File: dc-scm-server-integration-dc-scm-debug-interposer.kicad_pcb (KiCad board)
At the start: 6 copper layers, 90 x 62.3 mm, 164 parts, among them J1 Socket_DC-SCM-2.1_2x84_Rev-1-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, J10 PinHeader_2x5_P2.54mm_SMD, J11 PinHeader_2x5_P2.54mm_SMD, J12 PinHeader_2x5_P2.54mm_SMD, J13 PinHeader_2x5_P2.54mm_SMD, J15 Socket_SOP2-16_ACA-SPI-006-K0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, J16 Socket_SOP2-16_ACA-SPI-006-K0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, J17 PinHeader_2x5_P2.54mm_SMD, J2 PCB-Edge_DC-SCM-2.1_2x84_Rev-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, J3 PinHeader_2x5_P2.54mm_SMD, J4 PinHeader_2x5_P2.54mm_SMD, J5 PinHeader_2x5_P2.54mm_SMD, J6 PinHeader_2x5_P2.54mm_SMD, J7 PinHeader_2x5_P2.54mm_SMD, J9 PinHeader_2x5_P2.54mm_SMD, Q3 DMG1012T-7, U1 TLV76701_WSON

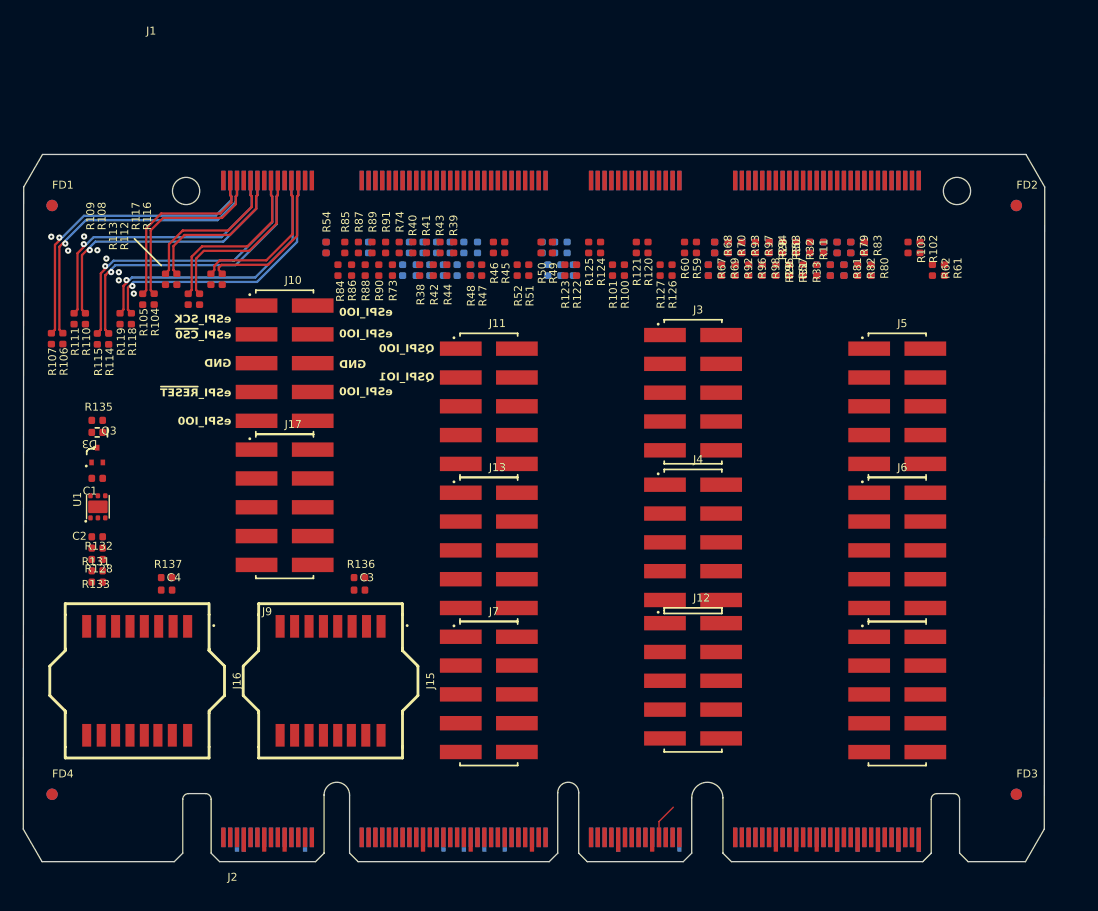
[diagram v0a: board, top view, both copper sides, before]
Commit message: [#100720] Start placing silkscreen labels
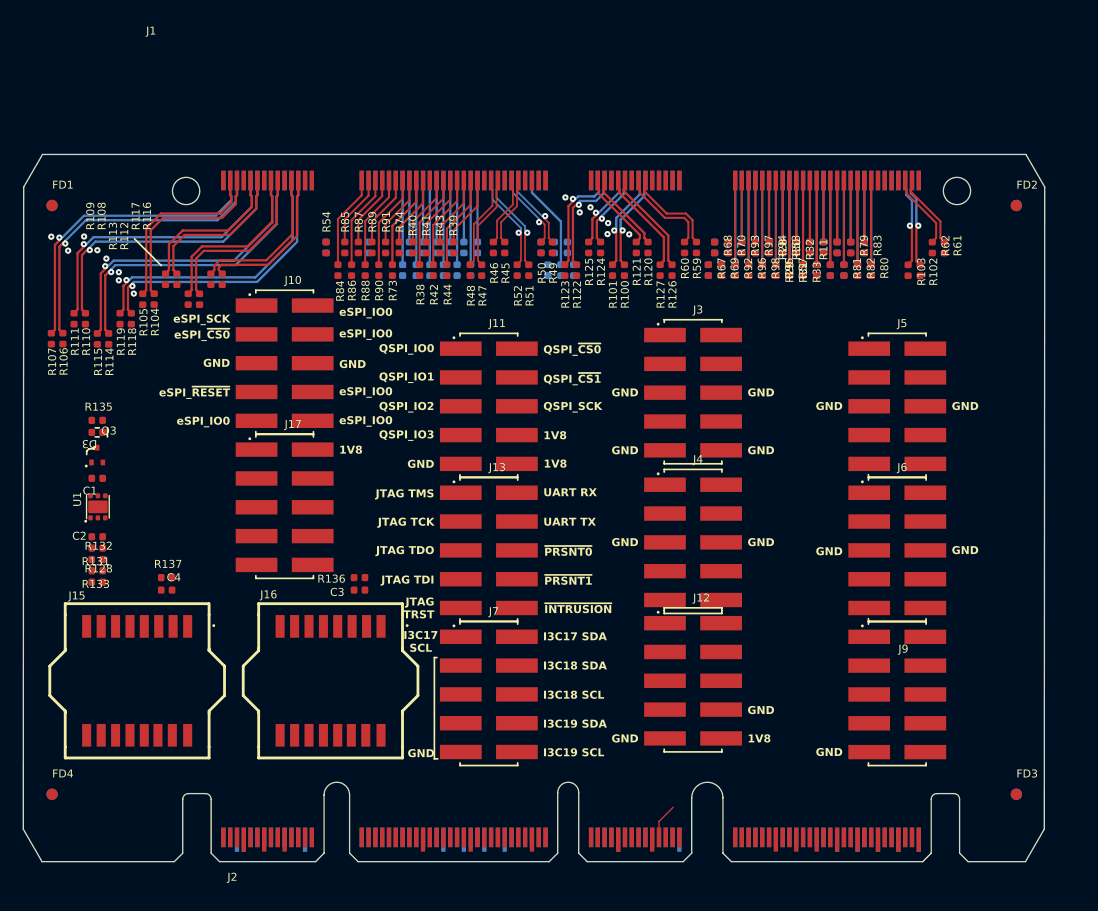
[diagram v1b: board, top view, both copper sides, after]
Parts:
- moved R102 2.01 mm to (179.0, 80.2)
- moved R103 2.01 mm to (178.0, 80.2)
- moved R61 1.99 mm to (181.1, 78.2)
- moved R62 1.99 mm to (180.1, 78.2)
- moved R3 0.10 mm to (145.6, 78.2)
- turned R99 to 90 degrees
- turned R14 to 90 degrees
- turned R15 to 90 degrees
- turned R16 to 90 degrees
- turned R18 to 90 degrees
- turned R20 to 90 degrees
- turned R21 to 90 degrees
- turned R22 to 90 degrees
- turned R23 to 90 degrees
- turned R24 to 90 degrees
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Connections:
- net Net-(J1A-USB2_SCMHOST1_DN) renamed /DC-SCI gold fingers connector/USB1_D-
- net Net-(J1A-USB2_SCMHOST1_DP) renamed /DC-SCI gold fingers connector/USB1_D+
- net Net-(J1A-USB2_SCMHOST2_DN) renamed /DC-SCI gold fingers connector/USB2_D-
- net Net-(J1A-USB2_SCMHOST2_DP) renamed /DC-SCI gold fingers connector/USB2_D+
- net Net-(J1C-LTPI_HPM_SCM_CLK_DN) renamed /DC-SCI gold fingers connector/LTPI_RXCK-
- net Net-(J1C-LTPI_HPM_SCM_CLK_DP) renamed /DC-SCI gold fingers connector/LTPI_RXCK+
- net Net-(J1C-LTPI_HPM_SCM_DATA_DN) renamed /DC-SCI gold fingers connector/LTPI_RXD-
- net Net-(J1C-LTPI_HPM_SCM_DATA_DP) renamed /DC-SCI gold fingers connector/LTPI_RXD+
- net Net-(J1C-LTPI_SCM_HPM_CLK_DN) renamed /DC-SCI gold fingers connector/LTPI_TXCK-
- net Net-(J1C-LTPI_SCM_HPM_CLK_DP) renamed /DC-SCI gold fingers connector/LTPI_TXCK+
- net Net-(J1C-LTPI_SCM_HPM_DATA_DN) renamed /DC-SCI gold fingers connector/LTPI_TXD-
- net Net-(J1C-LTPI_SCM_HPM_DATA_DP) renamed /DC-SCI gold fingers connector/LTPI_TXD+
- J1 pad A68: /DC-SCI gold fingers connector/CLK_100M_1_CLK+ -> /DC-SCI gold fingers connector/CLK_100M_1_CLK-
- R103 pad 1: /DC-SCI gold fingers connector/CLK_100M_1_CLK+ -> /DC-SCI gold fingers connector/CLK_100M_1_CLK-
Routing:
- net /DC-SCI gold fingers connector/PCIE1_RX0-: track 0.00 -> 9.69 mm, vias 0 -> 1
- net /DC-SCI gold fingers connector/PCIE1_RX0+: track 0.00 -> 9.69 mm, vias 0 -> 1
- net /DC-SCI gold fingers connector/PCIE_USB_SCMROOT_TX0+: track 0.00 -> 9.23 mm
- net /DC-SCI gold fingers connector/PCIE_USB_SCMROOT_TX0-: track 0.00 -> 9.23 mm
- net /DC-SCI gold fingers connector/LTPI_TXD-: track 0.00 -> 8.81 mm, vias 0 -> 1
- net /DC-SCI gold fingers connector/LTPI_TXD+: track 0.00 -> 8.81 mm, vias 0 -> 1
- net /DC-SCI gold fingers connector/CLK_100M_0_CLK-: track 0.00 -> 8.60 mm, vias 0 -> 1
- net /DC-SCI gold fingers connector/CLK_100M_0_CLK+: track 0.00 -> 8.60 mm, vias 0 -> 1
- net Net-(J1B-I2C_3V3_2_SCL): track 0.00 -> 8.48 mm
- net /DC-SCI gold fingers connector/USB1_D-: track 0.00 -> 8.37 mm
- net /DC-SCI gold fingers connector/USB1_D+: track 0.00 -> 8.37 mm
- net Net-(J1C-QSPI_HPMCNTRL_IO_1): track 0.00 -> 8.29 mm
- net Net-(J1C-QSPI_HPMCNTRL_CS0_N): track 0.00 -> 8.29 mm
- net Net-(J1C-ESPI_HPMCNTRL_RESET_N): track 0.00 -> 8.29 mm
- net Net-(J1C-ESPI_HPMCNTRL_IO_3): track 0.00 -> 8.29 mm
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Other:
- board text added: "1V8"
- board text added: "I3C17 SCL"
- board text added: "I3C17 SDA"
- board text added: "I3C18 SCL"
- board text added: "I3C18 SDA"
- board text added: "I3C19 SCL"
- board text added: "I3C19 SDA"
- board text added: "JTAG TCK"
- board text added: "JTAG TDI"
- board text added: "JTAG TDO"
- board text added: "JTAG TMS"
- board text added: "JTAG TRST"
- board text added: "QSPI_IO2"
- board text added: "QSPI_IO3"
- board text added: "QSPI_SCK"
- board text added: "QSPI_~{CS0}"
- board text added: "QSPI_~{CS1}"
- board text added: "UART RX"
- board text added: "UART TX"
- board text added: "~{INTRUSION}"
- board text added: "~{PRSNT0}"
- board text added: "~{PRSNT1}"

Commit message: [#100720] Finish silkscreen
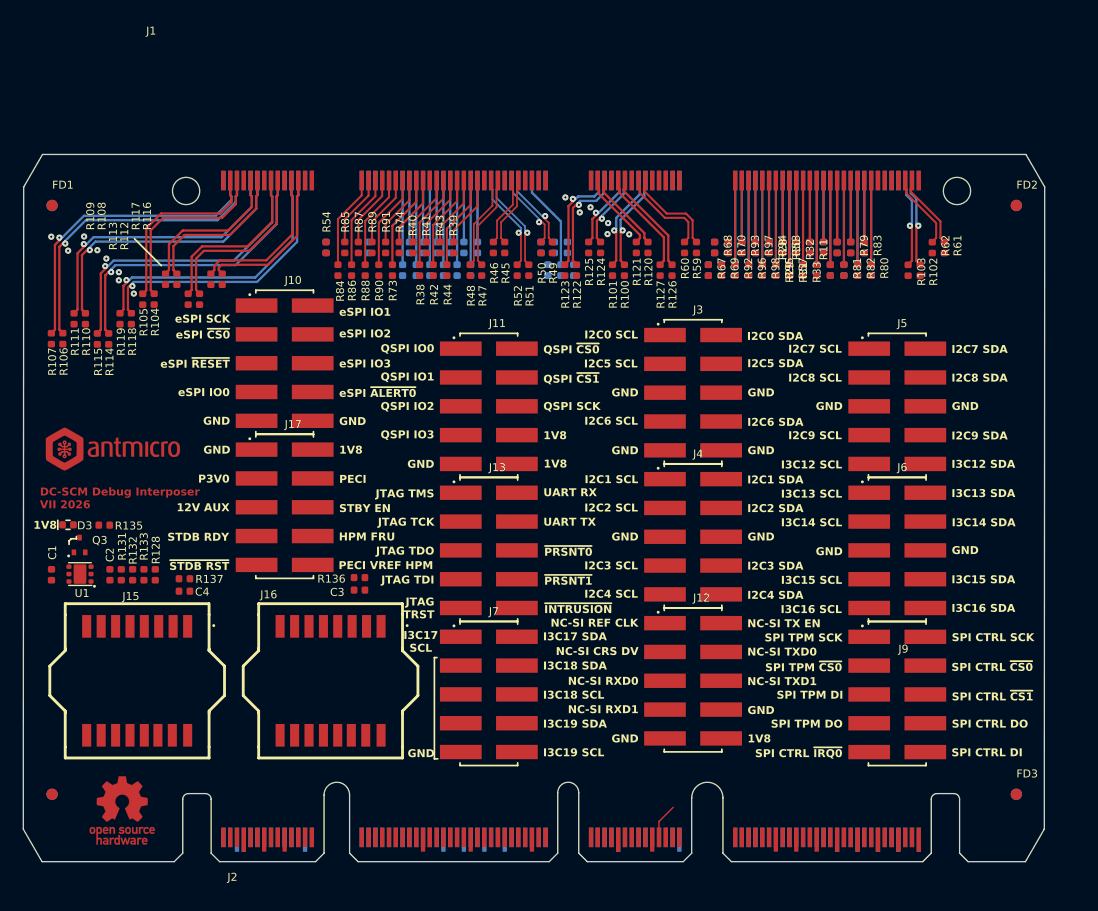
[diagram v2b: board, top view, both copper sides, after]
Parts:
- added REF**: OSHW-Logo_5.7x6mm_Copper, antmicro-footprints:OSHW-Logo_5.7x6mm_Copper, F.Cu at (108.7, 127.8)
- added REF**: LOGO, antmicro-footprints:antmicro-logo_scaled_12mm, F.Cu at (107.8, 96.0)
- added REF**: OSHW-Logo_5.7x6mm_Mask, antmicro-footprints:OSHW-Logo_5.7x6mm_Mask, F.Cu at (108.7, 127.8)
- moved C1 9.41 mm to (102.5, 107.0), turned to -90 degrees
- moved R135 9.26 mm to (107.1, 102.7)
- moved D3 8.55 mm to (103.9, 102.7), turned to 0 degrees
- moved Q3 8.08 mm to (104.9, 104.4)
- moved U1 6.14 mm to (105.0, 107.0), turned to 180 degrees
- moved R128 5.16 mm to (111.6, 107.0), turned to 90 degrees
- moved R133 4.13 mm to (110.6, 107.0), turned to -90 degrees
- moved C2 3.53 mm to (107.6, 107.0), turned to -90 degrees
- moved R132 3.40 mm to (109.6, 107.0), turned to 90 degrees
- moved R131 3.16 mm to (108.6, 107.0), turned to -90 degrees
- moved R137 1.57 mm to (114.2, 107.4)
- moved C4 1.57 mm to (114.2, 108.5)
- moved J4 0.49 mm to (159.0, 103.7)
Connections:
- J10 pad 10: /DC-SCI edge connector/DC_SCM_ESPI.~{ALERT0} -> GND
- J10 pad 5: GND -> /DC-SCI edge connector/DC_SCM_ESPI.~{RESET}
- J10 pad 6: GND -> /DC-SCI edge connector/DC_SCM_ESPI.IO3
- J10 pad 7: /DC-SCI edge connector/DC_SCM_ESPI.~{RESET} -> /DC-SCI edge connector/DC_SCM_ESPI.IO0
- J10 pad 8: /DC-SCI edge connector/DC_SCM_ESPI.IO3 -> /DC-SCI edge connector/DC_SCM_ESPI.~{ALERT0}
- J10 pad 9: /DC-SCI edge connector/DC_SCM_ESPI.IO0 -> GND
- J17 pad 1: /DC-SCI edge connector/DC_SCM_12V_AUX -> GND
- J17 pad 5: /DC-SCI edge connector/DC_SCM_STBY_RDY -> /DC-SCI edge connector/DC_SCM_12V_AUX
- J17 pad 7: /DC-SCI edge connector/~{DC_SCM_STBY_RST} -> /DC-SCI edge connector/DC_SCM_STBY_RDY
- J17 pad 9: /DC-SCI edge connector/~{DC_SCM_SPI_SCMCNTRL_IRQ0} -> /DC-SCI edge connector/~{DC_SCM_STBY_RST}
- J9 pad 9: GND -> /DC-SCI edge connector/~{DC_SCM_SPI_SCMCNTRL_IRQ0}
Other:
- board text added: "12V AUX"
- board text added: "DC-SCM Debug Interposer VII 2026"
- board text added: "HPM FRU"
- board text added: "I2C0 SCL"
- board text added: "I2C0 SDA"
- board text added: "I2C1 SCL"
- board text added: "I2C1 SDA"
- board text added: "I2C2 SCL"
- board text added: "I2C2 SDA"
- board text added: "I2C3 SCL"
- board text added: "I2C3 SDA"
- board text added: "I2C4 SCL"
- board text added: "I2C4 SDA"
- board text added: "I2C5 SCL"
- board text added: "I2C5 SDA"
- board text added: "I2C6 SCL"
- board text added: "I2C6 SDA"
- board text added: "I2C7 SCL"
- board text added: "I2C7 SDA"
- board text added: "I2C8 SCL"
- board text added: "I2C8 SDA"
- board text added: "I2C9 SCL"
- board text added: "I2C9 SDA"
- board text added: "I3C12 SCL"
- board text added: "I3C12 SDA"
- board text added: "I3C13 SCL"
- board text added: "I3C13 SDA"
- board text added: "I3C14 SCL"
- board text added: "I3C14 SDA"
- board text added: "I3C15 SCL"
- board text added: "I3C15 SDA"
- board text added: "I3C16 SCL"
- board text added: "I3C16 SDA"
- board text added: "NC-SI CRS DV"
- board text added: "NC-SI REF CLK"
- board text added: "NC-SI RXD0"
- board text added: "NC-SI RXD1"
- board text added: "NC-SI TX EN"
- board text added: "NC-SI TXD0"
- board text added: "NC-SI TXD1"
- board text added: "P3V0"
- board text added: "PECI"
- board text added: "PECI VREF HPM"
- board text added: "QSPI IO0"
- board text added: "QSPI IO1"
- board text added: "QSPI IO2"
- board text added: "QSPI IO3"
- board text added: "QSPI SCK"
- board text added: "QSPI ~{CS0}"
- board text added: "QSPI ~{CS1}"
- board text added: "SPI CTRL DI"
- board text added: "SPI CTRL DO"
- board text added: "SPI CTRL SCK"
- board text added: "SPI CTRL ~{CS0}"
- board text added: "SPI CTRL ~{CS1}"
- board text added: "SPI CTRL ~{IRQ0}"
- board text added: "SPI TPM DI"
- board text added: "SPI TPM DO"
- board text added: "SPI TPM SCK"
- board text added: "SPI TPM ~{CS0}"
- board text added: "STBY EN"
- board text added: "STDB RDY"
- board text added: "eSPI IO0"
- board text added: "eSPI IO1"
- board text added: "eSPI IO2"
- board text added: "eSPI IO3"
- board text added: "eSPI SCK"
- board text added: "eSPI ~{ALERT0}"
- board text added: "eSPI ~{CS0}"
- board text added: "eSPI ~{RESET}"
- board text added: "~{STDB RST}"
- board text removed: "QSPI_IO0"
- board text removed: "QSPI_IO1"
- board text removed: "QSPI_IO2"
- board text removed: "QSPI_IO3"
- board text removed: "QSPI_SCK"
- board text removed: "QSPI_~{CS0}"
- board text removed: "QSPI_~{CS1}"
- board text removed: "eSPI_IO0"
- board text removed: "eSPI_SCK"
- board text removed: "eSPI_~{CS0}"
- board text removed: "eSPI_~{RESET}"

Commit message: [#100720] Route high speeds
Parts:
- removed the REF** at (108.7, 127.8)
- J2: footprint antmicro-footprints:PCB-Edge_DC-SCM_2x84_Rev-1-0 -> antmicro-footprints:PCB-Edge_DC-SCM-2.1_2x84_Rev-1-1
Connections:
- J2 pad A51: /DC-SCI edge connector/DC_SCM_I2C_I3C16.SCL -> /DC-SCI edge connector/DC_SCM_I2C_I3C16.SDA
- J2 pad A52: /DC-SCI edge connector/DC_SCM_I2C_I3C16.SDA -> /DC-SCI edge connector/DC_SCM_I2C_I3C16.SCL
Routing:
- net /DC-SCI edge connector/DC_SCM_USB2.D-: track 0.00 -> 60.2 mm
- net /DC-SCI edge connector/DC_SCM_USB2.D+: track 0.00 -> 60.2 mm
- net /DC-SCI edge connector/DC_SCM_LTPI.RXCK+: track 0.00 -> 58.6 mm
- net /DC-SCI edge connector/DC_SCM_LTPI.RXCK-: track 0.00 -> 58.6 mm
- net /DC-SCI edge connector/DC_SCM_LTPI.RXD-: track 0.00 -> 57.1 mm
- net /DC-SCI edge connector/DC_SCM_LTPI.RXD+: track 0.00 -> 57.1 mm
- net /DC-SCI edge connector/DC-SCM_CLK_100M_1.CLK+: track 0.00 -> 56.8 mm, vias 0 -> 1
- net /DC-SCI edge connector/DC-SCM_CLK_100M_1.CLK-: track 0.00 -> 56.8 mm, vias 0 -> 1
- net /DC-SCI edge connector/DC-SCM_PCIE0_SGMII.RX1-: track 0.00 -> 56.5 mm, vias 0 -> 1
- net /DC-SCI edge connector/DC-SCM_PCIE0_SGMII.RX1+: track 0.00 -> 56.5 mm, vias 0 -> 1
- net /DC-SCI edge connector/DC-SCM_PCIE0_SGMII.RX3-: track 0.00 -> 55.9 mm, vias 0 -> 1
- net /DC-SCI edge connector/DC-SCM_PCIE0_SGMII.RX3+: track 0.00 -> 55.9 mm, vias 0 -> 1
- net /DC-SCI edge connector/DC_SCM_USB1.D-: track 0.00 -> 55.0 mm
- net /DC-SCI edge connector/DC_SCM_USB1.D+: track 0.00 -> 55.0 mm
- net /DC-SCI edge connector/DC-SCM_PCIE0_SGMII.RX0+: track 0.00 -> 54.9 mm, vias 0 -> 1
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
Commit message: [#100720] Start routing low speeds
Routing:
- net /DC-SCI edge connector/DC_SCM_HPM_FRU: track 0.00 -> 98.4 mm, vias 0 -> 2
- net /DC-SCI edge connector/DC_SCM_UART.TX: track 0.00 -> 82.8 mm, vias 0 -> 2
- net /DC-SCI edge connector/DC_SCM_UART.RX: track 0.00 -> 78.7 mm, vias 0 -> 2
- net /DC-SCI edge connector/DC_SCM_I2C_I3C18.SCL: track 0.00 -> 68.7 mm, vias 0 -> 2
- net /DC-SCI edge connector/DC_SCM_I2C_I3C19.SCL: track 0.00 -> 65.2 mm, vias 0 -> 2
- net /DC-SCI edge connector/DC_SCM_I2C_I3C18.SDA: track 0.00 -> 65.1 mm, vias 0 -> 2
- net /DC-SCI edge connector/DC_SCM_I2C_I3C19.SDA: track 0.00 -> 65.1 mm, vias 0 -> 2
- net /DC-SCI edge connector/DC_SCM_I2C7.SCL: track 0.00 -> 61.7 mm, vias 0 -> 2
- net /DC-SCI edge connector/DC_SCM_I2C7.SDA: track 0.00 -> 61.7 mm, vias 0 -> 2
- net /DC-SCI edge connector/DC_SCM_I2C_I3C16.SCL: track 0.00 -> 60.5 mm, vias 0 -> 2
- net /DC-SCI edge connector/DC_SCM_TPM_SPI.DI: track 0.00 -> 58.8 mm, vias 0 -> 2
- net /DC-SCI edge connector/DC_SCM_TPM_SPI.SCK: track 0.00 -> 58.6 mm, vias 0 -> 2
- net /DC-SCI edge connector/DC_SCM_I2C5.SCL: track 0.00 -> 58.4 mm, vias 0 -> 2
- net /DC-SCI edge connector/DC_SCM_I2C_I3C13.SDA: track 0.00 -> 58.0 mm, vias 0 -> 2
- net /DC-SCI edge connector/DC_SCM_I2C_I3C12.SDA: track 0.00 -> 57.6 mm, vias 0 -> 2
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
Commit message: [#100720] Continue routing low speeds
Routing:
- net GND: track 38.4 -> 138.9 mm, vias 42 -> 83
- net /DC-SCI edge connector/DC_SCM_STBY_EN: track 0.00 -> 78.9 mm, vias 0 -> 2
- net /DC-SCI edge connector/~{DC_SCM_STBY_RST}: track 0.00 -> 76.7 mm, vias 0 -> 2
- net /DC-SCI edge connector/DC_SCM_I2C_I3C14.SDA: track 0.00 -> 75.0 mm, vias 0 -> 4
- net /DC-SCI edge connector/DC_SCM_I2C0.SDA: track 0.00 -> 73.8 mm, vias 0 -> 2
- net /DC-SCI edge connector/DC_SCM_I2C_I3C15.SDA: track 0.00 -> 73.0 mm, vias 0 -> 4
- net /DC-SCI edge connector/DC_SCM_I2C0.SCL: track 0.00 -> 72.8 mm, vias 0 -> 2
- net /DC-SCI edge connector/DC_SCM_I2C1.SCL: track 0.00 -> 71.7 mm, vias 0 -> 2
- net /DC-SCI edge connector/DC_SCM_I2C_I3C14.SCL: track 0.00 -> 70.3 mm, vias 0 -> 4
- net /DC-SCI edge connector/DC_SCM_I2C_I3C15.SCL: track 0.00 -> 68.1 mm, vias 0 -> 4
- net /DC-SCI edge connector/DC_SCM_SPI_SCMCNTRL.~{CS1}: track 0.00 -> 62.9 mm, vias 0 -> 2
- net /DC-SCI edge connector/DC_SCM_I2C8.SCL: track 0.00 -> 62.6 mm, vias 0 -> 2
- net /DC-SCI edge connector/DC_SCM_NC-SI.RXD0: track 0.00 -> 61.8 mm, vias 0 -> 2
- net /DC-SCI edge connector/DC_SCM_I2C9.SCL: track 0.00 -> 61.5 mm, vias 0 -> 2
- net /DC-SCI edge connector/DC_SCM_I2C8.SDA: track 0.00 -> 61.2 mm, vias 0 -> 2
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- added copper zone on In1.Cu, net GND
- added copper zone on In2.Cu, net GND
- added copper zone on In4.Cu, net GND
